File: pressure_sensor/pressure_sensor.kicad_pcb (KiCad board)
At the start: 2 copper layers, 10 parts, among them J1 SCREW_TERM, J2 SCREW_TERM, P1 SWD_TC, U1 STM32F042K4, U2 MS580314BA01-00, U3 MCP2551-I/SN

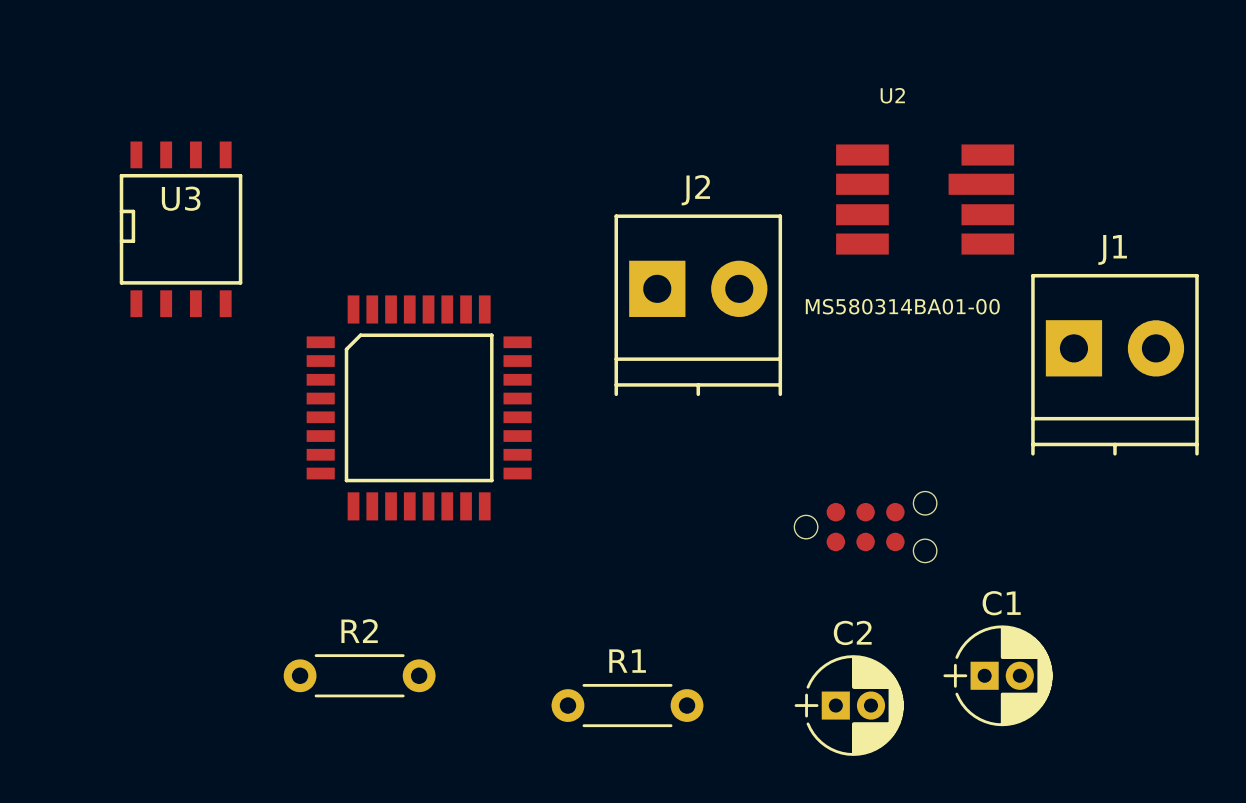
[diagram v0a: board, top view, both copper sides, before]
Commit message: finished pressure sensor board
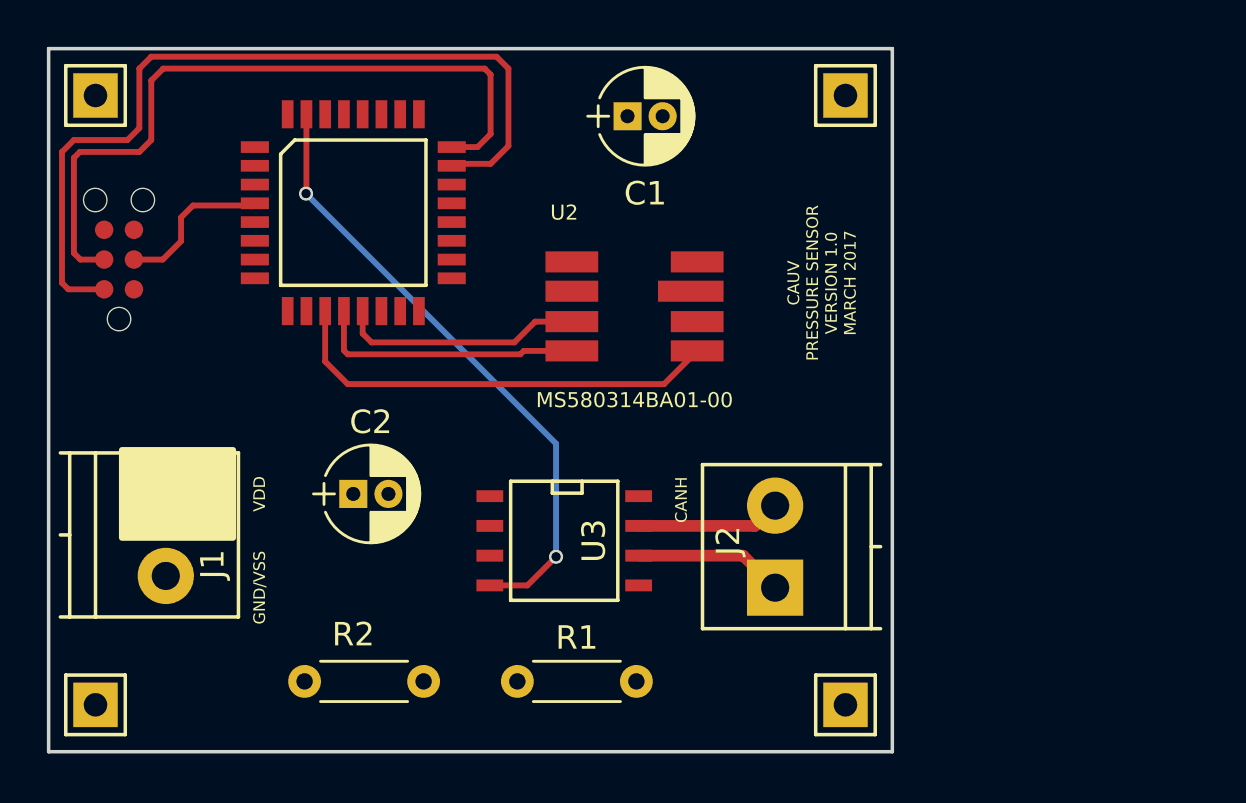
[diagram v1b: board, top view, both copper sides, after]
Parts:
- added J3: S1, agg:SIL-254P-01, F.Cu at (117.0, 113.0)
- added J4: S2, agg:SIL-254P-01, F.Cu at (149.0, 87.0)
- added J5: S3, agg:SIL-254P-01, F.Cu at (149.0, 113.0)
- added J6: S4, agg:SIL-254P-01, F.Cu at (117.0, 87.0)
- moved J1 39.2 mm to (120.0, 104.0), turned to 270 degrees
- moved P1 33.8 mm to (118.0, 94.0), turned to 90 degrees
- moved C1 28.3 mm to (139.7, 87.9)
- moved C2 22.5 mm to (128.0, 104.0)
- moved U3 21.1 mm to (137.0, 106.0), turned to 270 degrees
- moved J2 13.7 mm to (146.0, 108.0), turned to 90 degrees
- moved U2 13.2 mm to (140.0, 96.0)
- moved U1 8.79 mm to (128.0, 92.0)
- moved R2 5.28 mm to (131.0, 112.0), turned to 180 degrees
- moved R1 2.39 mm to (135.0, 112.0)
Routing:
- net /SWDIO: track 0.00 -> 36.0 mm
- net /SWDCLK: track 0.00 -> 30.8 mm
- net /CANRXD: track 0.00 -> 26.6 mm, vias 0 -> 2
- net /SPI_SCLK: track 0.00 -> 19.0 mm
- net /SPI_MISO: track 0.00 -> 11.5 mm
- net /SPI_MOSI: track 0.00 -> 10.4 mm
- net /NRST: track 0.00 -> 6.75 mm
- net /CANL: track 0.00 -> 6.39 mm
- net /CANH: track 0.00 -> 6.18 mm
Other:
- board outline added: 36 x 30 mm
- board text added: "CANH"
- board text added: "CAUV PRESSURE SENSOR VERSION 1.0 MARCH 2017"
- board text added: "GND/VSS"
- board text added: "VDD"

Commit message: finished pressure sensor
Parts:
- P1: footprint agg:TC2030-NL -> footprints:SWD_CONN
- U2: footprint MS580314BA01-00:XDCR_MS580314BA01-00 -> footprints:XDCR_MS580314BA01-00
- moved P1 1.15 mm to (119.1, 94.2)
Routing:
- net /VDD: track 0.00 -> 75.2 mm, vias 0 -> 2
- net /VSS: track 0.00 -> 24.6 mm, vias 0 -> 2
- net /CANTXD: track 0.00 -> 18.7 mm, vias 0 -> 2
- net Net-(R1-Pad2): track 0.00 -> 16.9 mm
- net /CANRXD: track 26.6 -> 30.5 mm
- net /SWDCLK: track 30.8 -> 29.5 mm
- net /SWDIO: track 36.0 -> 36.9 mm
- net /NRST: track 6.75 -> 5.88 mm
- added copper zone on B.Cu, net /VSS
- added copper zone on F.Cu, net /VSS

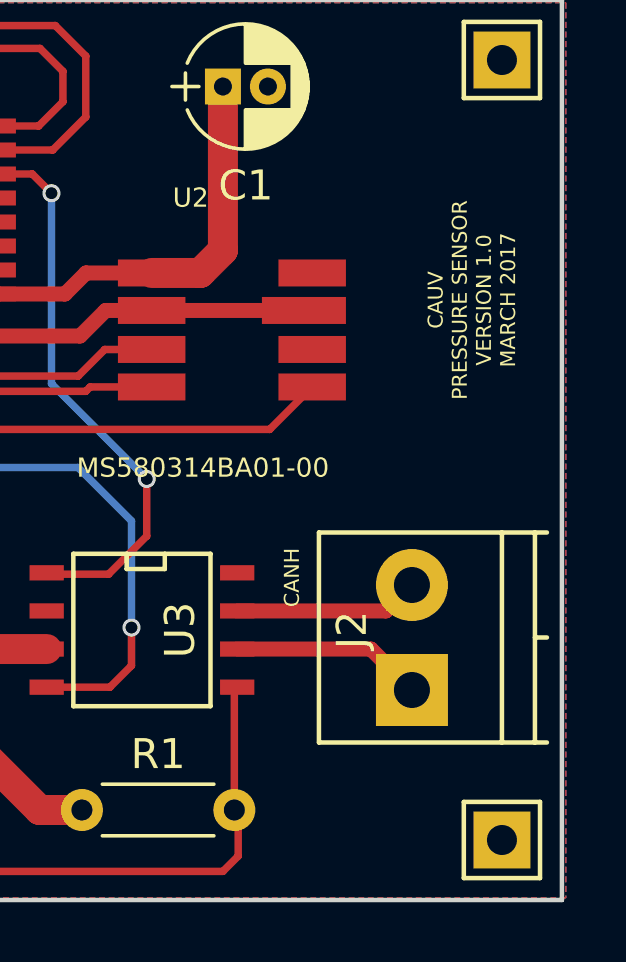
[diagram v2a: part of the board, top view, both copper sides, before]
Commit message: added logo to sensor
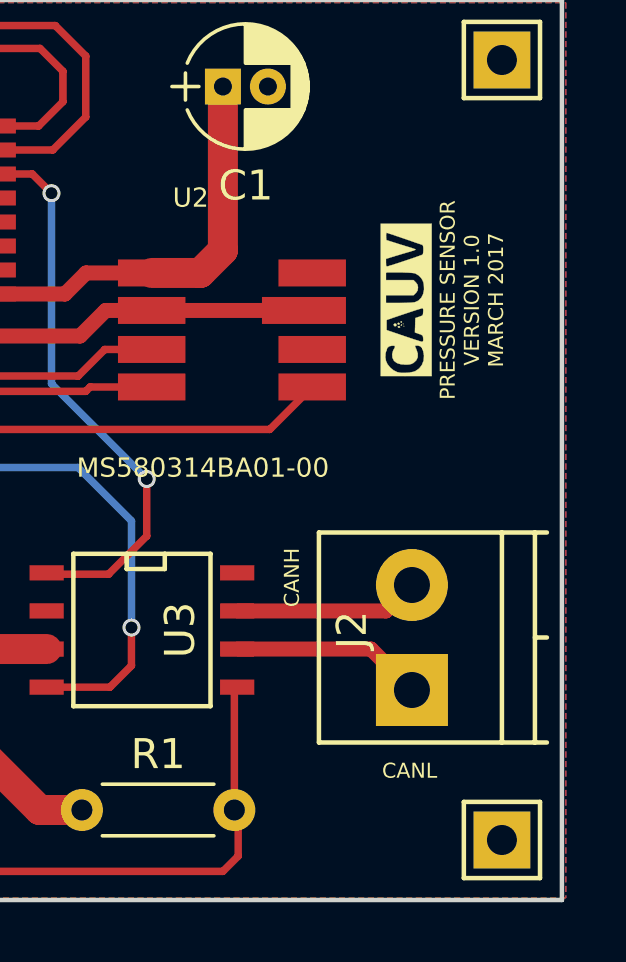
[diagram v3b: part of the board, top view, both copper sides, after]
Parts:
- added G***: LOGO, footprints:LOGO, F.Cu at (145.8, 95.0)
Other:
- board text added: "CANL"
- board text added: "PRESSURE SENSOR VERSION 1.0 MARCH 2017"
- board text removed: "CAUV PRESSURE SENSOR VERSION 1.0 MARCH 2017"
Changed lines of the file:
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@@
     (links 32)
     (no_connects 0)
-    (area 114.924999 84.924999 151.075001 115.075001)
+    (area 114.924999 84.924999 151.130001 115.075001)
     (thickness 1.6)
-    (drawings 11)
+    (drawings 12)
     (tracks 132)
     (zones 0)
-    (modules 14)
+    (modules 15)
     (nets 38)
   )
   (page A4)
   (layers
-    (0 F.Cu signal hide)
-    (31 B.Cu signal hide)
+    (0 F.Cu signal)
+    (31 B.Cu signal)
     (32 B.Adhes user hide)
     (33 F.Adhes user hide)
     (34 B.Paste user hide)
     (35 F.Paste user hide)
-    (36 B.SilkS user hide)
+    (36 B.SilkS user)
     (37 F.SilkS user)
     (38 B.Mask user hide)
@@
   )
   (setup
-    (last_trace_width 1.5)
+    (last_trace_width 0.25)
     (user_trace_width 0.25)
     (user_trace_width 0.5)
@@
       (net 29 /SPI_SCLK) (solder_mask_margin 0.2))
   )
+  (module footprints:LOGO (layer F.Cu)
+    (at 145.796 94.996 90)
+    (fp_text reference G*** (at 0 2.54 90) (layer F.SilkS) hide
+      (effects (font (thickness 0.3)))
+    )
+    (fp_text value LOGO (at 1.27 -2.54 90) (layer F.SilkS) hide
+      (effects (font (thickness 0.3)))
+    )
+    (fp_poly (pts (xy 2.54 0.8636) (xy -2.54 0.8636) (xy -2.54 -0.028103) (xy -2.432723 -0.028103)
+      (xy -2.422757 0.11072) (xy -2.400895 0.235486) (xy -2.373865 0.316095) (xy -2.286897 0.443908)
+      (xy -2.167904 0.536711) (xy -2.024292 0.591524) (xy -1.863467 0.605363) (xy -1.7145 0.581533)
+      (xy -1.642836 0.55391) (xy -1.397405 0.55391) (xy -1.378204 0.575531) (xy -1.31764 0.580814)
+      (xy -1.289215 0.57931) (xy -1.226933 0.572276) (xy -1.189225 0.554331) (xy -1.16241 0.513011)
+      (xy -1.133317 0.437272) (xy -1.085206 0.303044) (xy -0.845004 0.310272) (xy -0.604803 0.3175)
+      (xy -0.562752 0.4445) (xy -0.536341 0.518408) (xy -0.510233 0.556945) (xy -0.468867 0.572999)
+      (xy -0.40005 0.579241) (xy -0.326522 0.581203) (xy -0.29112 0.572073) (xy -0.28168 0.54793)
+      (xy -0.281826 0.541141) (xy -0.290443 0.504888) (xy -0.313314 0.42793) (xy -0.348108 0.317577)
+      (xy -0.392494 0.181141) (xy -0.44414 0.025932) (xy -0.478676 -0.0762) (xy -0.6731 -0.6477)
+      (xy -1.002676 -0.6477) (xy -1.106941 -0.3429) (xy -1.193076 -0.090105) (xy -1.262961 0.117256)
+      (xy -1.317381 0.28161) (xy -1.357121 0.40538) (xy -1.382966 0.490992) (xy -1.395703 0.540871)
+      (xy -1.397405 0.55391) (xy -1.642836 0.55391) (xy -1.609454 0.541043) (xy -1.548284 0.48597)
+      (xy -1.524748 0.410031) (xy -1.524 0.389763) (xy -1.526605 0.332543) (xy -1.532972 0.305193)
+      (xy -1.533927 0.3048) (xy -1.560837 0.314374) (xy -1.618035 0.338706) (xy -1.654577 0.355042)
+      (xy -1.794246 0.39946) (xy -1.915135 0.396906) (xy -2.018433 0.347115) (xy -2.101088 0.256223)
+      (xy -2.134779 0.19416) (xy -2.152647 0.123156) (xy -2.158807 0.024683) (xy -2.159 -0.004573)
+      (xy -2.147449 -0.164747) (xy -2.111093 -0.286502) (xy -2.047379 -0.377088) (xy -2.018953 -0.402136)
+      (xy -1.924534 -0.446647) (xy -1.811813 -0.455255) (xy -1.698629 -0.427757) (xy -1.656737 -0.406306)
+      (xy -1.583999 -0.366879) (xy -1.543574 -0.362199) (xy -1.527942 -0.395483) (xy -1.52889 -0.461011)
+      (xy -1.546878 -0.548084) (xy -1.590764 -0.606191) (xy -1.600561 -0.613899) (xy -1.686865 -0.654052)
+      (xy -1.720385 -0.6604) (xy -0.1016 -0.6604) (xy -0.101459 -0.22225) (xy -0.099907 -0.070711)
+      (xy -0.095702 0.069739) (xy -0.089374 0.188395) (xy -0.081451 0.274552) (xy -0.075155 0.3101)
+      (xy -0.017955 0.427237) (xy 0.076703 0.517925) (xy 0.201164 0.579066) (xy 0.347771 0.607565)
+      (xy 0.508868 0.600325) (xy 0.595708 0.58144) (xy 0.710228 0.52593) (xy 0.808502 0.434809)
+      (xy 0.875353 0.323255) (xy 0.88624 0.290908) (xy 0.895696 0.231577) (xy 0.903796 0.132584)
+      (xy 0.909947 0.005061) (xy 0.913556 -0.139859) (xy 0.914258 -0.23495) (xy 0.914394 -0.645233)
+      (xy 1.110899 -0.645233) (xy 1.115473 -0.619223) (xy 1.134136 -0.553182) (xy 1.164242 -0.455048)
+      (xy 1.20315 -0.332755) (xy 1.248216 -0.194241) (xy 1.296796 -0.04744) (xy 1.346249 0.099711)
+      (xy 1.393931 0.239276) (xy 1.437198 0.36332) (xy 1.473408 0.463906) (xy 1.499918 0.533099)
+      (xy 1.512619 0.560934) (xy 1.543894 0.573482) (xy 1.609977 0.581929) (xy 1.674936 0.5842)
+      (xy 1.762549 0.581111) (xy 1.811559 0.569652) (xy 1.833909 0.546536) (xy 1.836377 0.53975)
+      (xy 1.848336 0.503748) (xy 1.874461 0.427191) (xy 1.912197 0.317494) (xy 1.95899 0.182071)
+      (xy 2.012285 0.028338) (xy 2.042539 -0.058732) (xy 2.097467 -0.217739) (xy 2.146298 -0.361105)
+      (xy 2.186674 -0.481748) (xy 2.216242 -0.572585) (xy 2.232643 -0.626531) (xy 2.2352 -0.637974)
+      (xy 2.212364 -0.651523) (xy 2.153321 -0.656669) (xy 2.11455 -0.655442) (xy 1.9939 -0.6477)
+      (xy 1.901402 -0.3556) (xy 1.857781 -0.216614) (xy 1.812986 -0.071824) (xy 1.773142 0.058873)
+      (xy 1.75088 0.13335) (xy 1.722137 0.224566) (xy 1.696933 0.293343) (xy 1.679624 0.328123)
+      (xy 1.676665 0.3302) (xy 1.663005 0.307511) (xy 1.640453 0.246952) (xy 1.613032 0.159784)
+      (xy 1.601787 0.12065) (xy 1.568709 0.005256) (xy 1.526758 -0.13722) (xy 1.482273 -0.285391)
+      (xy 1.454993 -0.374651) (xy 1.366887 -0.660401) (xy 1.246477 -0.660401) (xy 1.172406 -0.657452)
+      (xy 1.121703 -0.649975) (xy 1.110899 -0.645233) (xy 0.914394 -0.645233) (xy 0.9144 -0.6604)
+      (xy 0.6604 -0.6604) (xy 0.6604 0.257907) (xy 0.586153 0.332153) (xy 0.517526 0.385562)
+      (xy 0.440731 0.405241) (xy 0.4064 0.4064) (xy 0.319794 0.39569) (xy 0.251635 0.355497)
+      (xy 0.226646 0.332153) (xy 0.1524 0.257907) (xy 0.1524 -0.6604) (xy -0.1016 -0.6604)
+      (xy -1.720385 -0.6604) (xy -1.80246 -0.675943) (xy -1.928494 -0.677523) (xy -2.032 -0.660772)
+      (xy -2.14594 -0.608208) (xy -2.255281 -0.519334) (xy -2.346657 -0.407883) (xy -2.406703 -0.287582)
+      (xy -2.411943 -0.270477) (xy -2.429538 -0.161622) (xy -2.432723 -0.028103) (xy -2.54 -0.028103)
+      (xy -2.54 -0.8382) (xy 2.54 -0.8382) (xy 2.54 0.8636)) (layer F.SilkS) (width 0.01))
+    (fp_poly (pts (xy -0.8636 -0.0635) (xy -0.8763 -0.0508) (xy -0.889 -0.0635) (xy -0.8763 -0.0762)
+      (xy -0.8636 -0.0635)) (layer F.SilkS) (width 0.01))
+    (fp_poly (pts (xy -0.7874 -0.0889) (xy -0.8001 -0.0762) (xy -0.8128 -0.0889) (xy -0.8001 -0.1016)
+      (xy -0.7874 -0.0889)) (layer F.SilkS) (width 0.01))
+    (fp_poly (pts (xy -0.8382 -0.1651) (xy -0.813969 -0.142276) (xy -0.8128 -0.138201) (xy -0.832452 -0.127292)
+      (xy -0.8382 -0.127) (xy -0.862624 -0.146527) (xy -0.8636 -0.1539) (xy -0.84804 -0.169069)
+      (xy -0.8382 -0.1651)) (layer F.SilkS) (width 0.01))
+    (fp_poly (pts (xy -0.711939 -0.158472) (xy -0.7112 -0.1524) (xy -0.730529 -0.127739) (xy -0.7366 -0.127)
+      (xy -0.761262 -0.146329) (xy -0.762 -0.1524) (xy -0.742672 -0.177062) (xy -0.7366 -0.1778)
+      (xy -0.711939 -0.158472)) (layer F.SilkS) (width 0.01))
+    (fp_poly (pts (xy -0.8763 -0.254) (xy -0.874454 -0.211892) (xy -0.883267 -0.198774) (xy -0.914404 -0.189659)
+      (xy -0.9271 -0.2032) (xy -0.928947 -0.245309) (xy -0.920134 -0.258427) (xy -0.888997 -0.267542)
+      (xy -0.8763 -0.254)) (layer F.SilkS) (width 0.01))
+    (fp_poly (pts (xy -0.76469 -0.258805) (xy -0.762 -0.2413) (xy -0.777599 -0.20627) (xy -0.812668 -0.212547)
+      (xy -0.820577 -0.219443) (xy -0.825713 -0.251106) (xy -0.799969 -0.276778) (xy -0.785901 -0.2794)
+      (xy -0.76469 -0.258805)) (layer F.SilkS) (width 0.01))
+    (fp_poly (pts (xy -0.794329 -0.385252) (xy -0.7874 -0.3556) (xy -0.805476 -0.314738) (xy -0.843973 -0.305813)
+      (xy -0.8763 -0.3302) (xy -0.879611 -0.372804) (xy -0.84658 -0.402583) (xy -0.824001 -0.4064)
+      (xy -0.794329 -0.385252)) (layer F.SilkS) (width 0.01))
+  )
+  (gr_text CANL (at 145.923 110.6932) (layer F.SilkS)
+    (effects (font (size 0.5 0.5) (thickness 0.125)))
+  )
   (gr_line (start 120.396 98.806) (end 121.158 99.568) (angle 90) (layer F.SilkS) (width 0.2))
   (gr_line (start 120.396 98.806) (end 119.634 99.568) (angle 90) (layer F.SilkS) (width 0.2))
@@
     (effects (font (size 0.5 0.5) (thickness 0.125)))
   )
-  (gr_text "CAUV\nPRESSURE SENSOR\nVERSION 1.0\nMARCH 2017" (at 148 95 90) (layer F.SilkS)
+  (gr_text "PRESSURE SENSOR\nVERSION 1.0\nMARCH 2017" (at 148 95 90) (layer F.SilkS)
     (effects (font (size 0.5 0.5) (thickness 0.125)))
   )
